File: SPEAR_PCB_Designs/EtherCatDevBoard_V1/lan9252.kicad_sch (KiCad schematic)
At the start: 29 parts, among them U4 LAN9252I/ML, Y2 25MHz

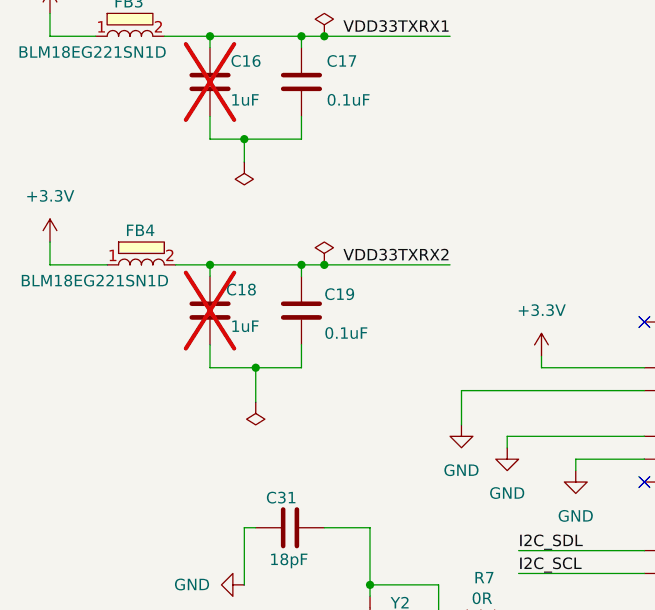
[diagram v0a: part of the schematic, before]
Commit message: Henry's continued work on the EtherCAT microcontroller dev. board.
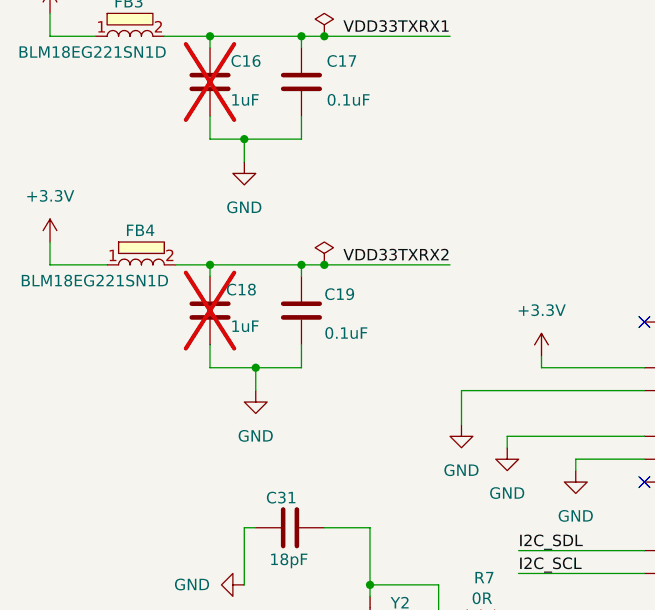
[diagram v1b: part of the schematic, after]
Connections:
- net GND: now also C16.2, C17.2, C18.2, C19.2
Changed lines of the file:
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@@
 	(wire
 		(pts
-			(xy 41.91 63.5) (xy 41.91 59.69)
+			(xy 41.91 62.23) (xy 41.91 59.69)
 		)
 		(stroke
@@
 	)
 	(symbol
-		(lib_id "power:PWR_FLAG")
-		(at 40.64 36.83 180)
-		(unit 1)
-		(exclude_from_sim no)
-		(in_bom yes)
-		(on_board yes)
-		(dnp no)
-		(fields_autoplaced yes)
-		(property "Reference" "#FLG06"
-			(at 40.64 38.735 0)
-			(effects
-				(font
-					(size 1.27 1.27)
-				)
-				(hide yes)
-			)
-		)
-		(property "Value" "PWR_FLAG"
-			(at 40.64 41.91 0)
-			(effects
-				(font
-					(size 1.27 1.27)
-				)
-				(hide yes)
-			)
-		)
-		(property "Footprint" ""
-			(at 40.64 36.83 0)
-			(effects
-				(font
-					(size 1.27 1.27)
-				)
-				(hide yes)
-			)
-		)
-		(property "Datasheet" "~"
-			(at 40.64 36.83 0)
-			(effects
-				(font
-					(size 1.27 1.27)
-				)
-				(hide yes)
-			)
-		)
-		(property "Description" "Special symbol for telling ERC where power comes from"
-			(at 40.64 36.83 0)
-			(effects
-				(font
-					(size 1.27 1.27)
-				)
-				(hide yes)
-			)
-		)
-		(pin "1"
-		)
-		(instances
-			(project "SPEAR_V1"
-				(path "/6af343d7-7346-4b6a-90ee-eb113982f4e5/d630782a-bbb8-450e-a52a-35375a587c4e"
-					(reference "#FLG06")
-					(unit 1)
-				)
-			)
-		)
-	)
-	(symbol
 		(lib_id "Device:C")
 		(at 231.14 63.5 0)
@@
 	)
 	(symbol
-		(lib_id "power:PWR_FLAG")
-		(at 41.91 63.5 180)
+		(lib_id "power:GND")
+		(at 40.64 36.83 0)
 		(unit 1)
 		(exclude_from_sim no)
@@
 		(dnp no)
 		(fields_autoplaced yes)
-		(property "Reference" "#FLG010"
-			(at 41.91 65.405 0)
+		(property "Reference" "#PWR059"
+			(at 40.64 43.18 0)
 			(effects
 				(font
@@
 			)
 		)
-		(property "Value" "PWR_FLAG"
-			(at 41.91 68.58 0)
+		(property "Value" "GND"
+			(at 40.64 41.91 0)
 			(effects
 				(font
 					(size 1.27 1.27)
 				)
-				(hide yes)
 			)
 		)
 		(property "Footprint" ""
-			(at 41.91 63.5 0)
+			(at 40.64 36.83 0)
 			(effects
 				(font
@@
 			)
 		)
-		(property "Datasheet" "~"
-			(at 41.91 63.5 0)
+		(property "Datasheet" ""
+			(at 40.64 36.83 0)
 			(effects
 				(font
@@
 			)
 		)
-		(property "Description" "Special symbol for telling ERC where power comes from"
-			(at 41.91 63.5 0)
+		(property "Description" "Power symbol creates a global label with name \"GND\" , ground"
+			(at 40.64 36.83 0)
 			(effects
 				(font
@@
 		)
 		(instances
-			(project "SPEAR_V1"
+			(project ""
 				(path "/6af343d7-7346-4b6a-90ee-eb113982f4e5/d630782a-bbb8-450e-a52a-35375a587c4e"
-					(reference "#FLG010")
+					(reference "#PWR059")
 					(unit 1)
 				)
@@
 					(unit 1)
 				)
+			)
+		)
+	)
+	(symbol
+		(lib_id "power:GND")
+		(at 41.91 62.23 0)
+		(unit 1)
+		(exclude_from_sim no)
+		(in_bom yes)
+		(on_board yes)
+		(dnp no)
+		(fields_autoplaced yes)
+		(property "Reference" "#PWR060"
+			(at 41.91 68.58 0)
+			(effects
+				(font
+					(size 1.27 1.27)
+				)
+				(hide yes)
+			)
+		)
+		(property "Value" "GND"
+			(at 41.91 67.31 0)
+			(effects
+				(font
+					(size 1.27 1.27)
+				)
+			)
+		)
+		(property "Footprint" ""
+			(at 41.91 62.23 0)
+			(effects
+				(font
+					(size 1.27 1.27)
+				)
+				(hide yes)
+			)
+		)
+		(property "Datasheet" ""
+			(at 41.91 62.23 0)
+			(effects
+				(font
+					(size 1.27 1.27)
+				)
+				(hide yes)
+			)
+		)
+		(property "Description" "Power symbol creates a global label with name \"GND\" , ground"
+			(at 41.91 62.23 0)
+			(effects
+				(font
+					(size 1.27 1.27)
+				)
+				(hide yes)
+			)
+		)
+		(pin "1"
+		)
+		(instances
+			(project "SPEAR_V1"
+				(path "/6af343d7-7346-4b6a-90ee-eb113982f4e5/d630782a-bbb8-450e-a52a-35375a587c4e"
+					(reference "#PWR060")
+					(unit 1)
+				)

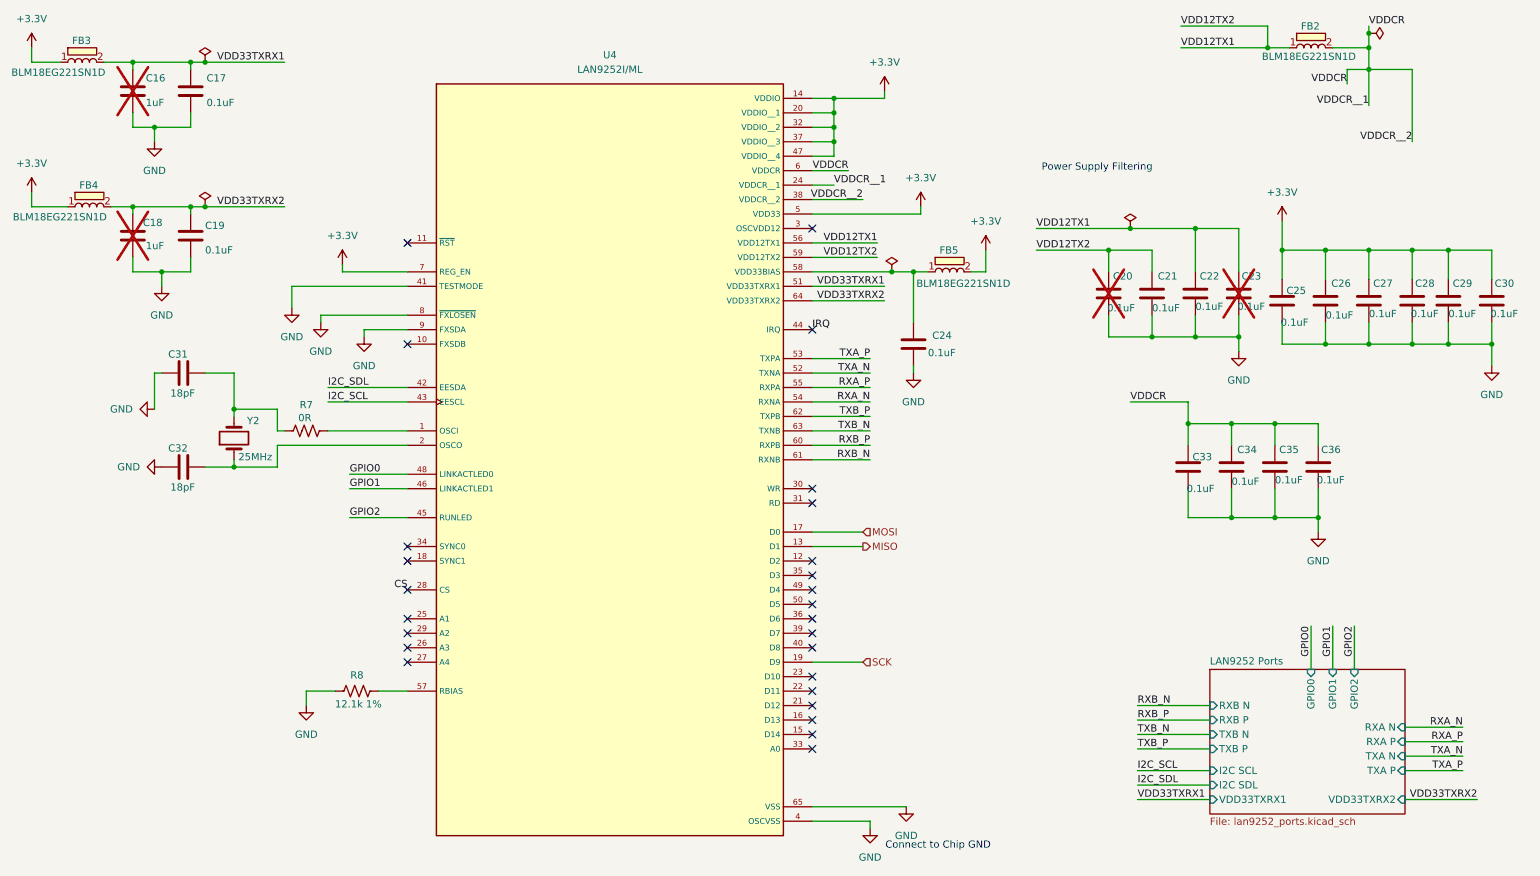
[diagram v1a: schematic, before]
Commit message: Edited schematic to fix problems with Lan9252. Continued work on pcb layout.
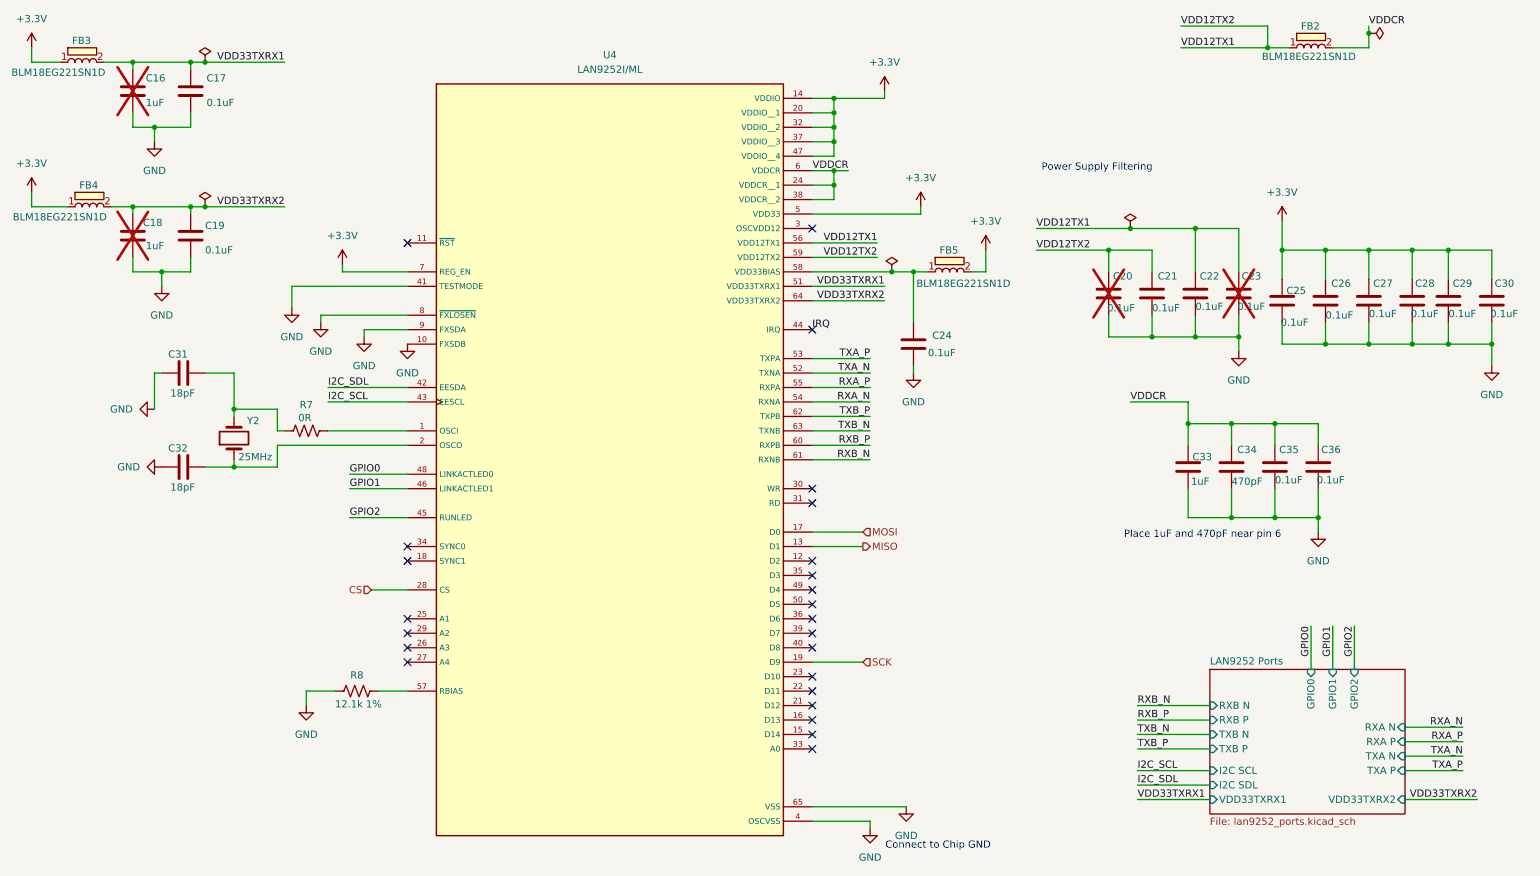
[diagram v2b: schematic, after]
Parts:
- C33: value 0.1uF -> 1uF
- C34: value 0.1uF -> 470pF
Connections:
- net GND: now also U4.10 (FXSDB)
- no-connect marks 26 -> 24
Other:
- note added: "Place 1uF and 470pF near pin 6"
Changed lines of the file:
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@@
 	(generator_version "9.0")
 	(paper "A4")
+	(text "Place 1uF and 470pF near pin 6"
+		(exclude_from_sim no)
+		(at 224.79 105.918 0)
+		(effects
+			(font
+				(size 1.27 1.27)
+			)
+		)
+	)
 	(text "Connect to Chip GND"
 		(exclude_from_sim no)
@@
 	)
 	(junction
-		(at 254 20.32)
-		(diameter 0)
-		(color 0 0 0 0)
-	)
-	(junction
-		(at 254 24.13)
-		(diameter 0)
-		(color 0 0 0 0)
-	)
-	(junction
 		(at 237.49 86.36)
 		(diameter 0)
@@
 	)
 	(junction
+		(at 160.02 44.45)
+		(diameter 0)
+		(color 0 0 0 0)
+	)
+	(junction
 		(at 46.99 22.86)
 		(diameter 0)
@@
 	)
 	(junction
+		(at 160.02 41.91)
+		(diameter 0)
+		(color 0 0 0 0)
+	)
+	(junction
 		(at 229.87 86.36)
 		(diameter 0)
@@
 	)
 	(no_connect
-		(at 85.09 115.57)
-	)
-	(no_connect
 		(at 156.21 115.57)
 	)
@@
 	)
 	(no_connect
-		(at 85.09 72.39)
-	)
-	(no_connect
 		(at 156.21 143.51)
 	)
@@
 	(wire
 		(pts
-			(xy 250.19 26.67) (xy 250.19 24.13)
-		)
-		(stroke
-			(width 0)
-			(type default)
-		)
-	)
-	(wire
-		(pts
 			(xy 40.64 36.83) (xy 40.64 34.29)
 		)
@@
 	(wire
 		(pts
+			(xy 78.74 115.57) (xy 85.09 115.57)
+		)
+		(stroke
+			(width 0)
+			(type default)
+		)
+	)
+	(wire
+		(pts
 			(xy 275.59 55.88) (xy 275.59 60.96)
 		)
@@
 	(wire
 		(pts
+			(xy 160.02 41.91) (xy 160.02 44.45)
+		)
+		(stroke
+			(width 0)
+			(type default)
+		)
+	)
+	(wire
+		(pts
 			(xy 213.36 149.86) (xy 226.06 149.86)
 		)
@@
 	(wire
 		(pts
-			(xy 165.1 46.99) (xy 156.21 46.99)
+			(xy 156.21 46.99) (xy 160.02 46.99)
 		)
 		(stroke
@@
 	(wire
 		(pts
-			(xy 261.62 24.13) (xy 261.62 36.83)
-		)
-		(stroke
-			(width 0)
-			(type default)
-		)
-	)
-	(wire
-		(pts
 			(xy 270.51 139.7) (xy 260.35 139.7)
 		)
@@
 	(wire
 		(pts
-			(xy 254 24.13) (xy 254 30.48)
-		)
-		(stroke
-			(width 0)
-			(type default)
-		)
-	)
-	(wire
-		(pts
 			(xy 40.64 34.29) (xy 46.99 34.29)
 		)
@@
 	(wire
 		(pts
+			(xy 160.02 46.99) (xy 160.02 44.45)
+		)
+		(stroke
+			(width 0)
+			(type default)
+		)
+	)
+	(wire
+		(pts
 			(xy 213.36 147.32) (xy 226.06 147.32)
 		)
@@
 	(wire
 		(pts
-			(xy 162.56 41.91) (xy 156.21 41.91)
+			(xy 162.56 41.91) (xy 160.02 41.91)
 		)
 		(stroke
@@
 	(wire
 		(pts
-			(xy 254 20.32) (xy 254 24.13)
-		)
-		(stroke
-			(width 0)
-			(type default)
-		)
-	)
-	(wire
-		(pts
 			(xy 46.99 48.26) (xy 46.99 49.53)
 		)
@@
 	(wire
 		(pts
-			(xy 254 24.13) (xy 261.62 24.13)
-		)
-		(stroke
-			(width 0)
-			(type default)
-		)
-	)
-	(wire
-		(pts
 			(xy 223.52 59.69) (xy 223.52 52.07)
 		)
@@
 	(wire
 		(pts
-			(xy 250.19 24.13) (xy 254 24.13)
+			(xy 246.38 55.88) (xy 246.38 60.96)
 		)
 		(stroke
@@
 	(wire
 		(pts
-			(xy 246.38 55.88) (xy 246.38 60.96)
+			(xy 222.25 102.87) (xy 229.87 102.87)
 		)
 		(stroke
@@
 	(wire
 		(pts
-			(xy 222.25 102.87) (xy 229.87 102.87)
+			(xy 54.61 77.47) (xy 54.61 83.82)
 		)
 		(stroke
@@
 	(wire
 		(pts
-			(xy 54.61 77.47) (xy 54.61 83.82)
+			(xy 165.1 128.27) (xy 156.21 128.27)
 		)
 		(stroke
@@
 	(wire
 		(pts
-			(xy 165.1 128.27) (xy 156.21 128.27)
+			(xy 247.65 121.92) (xy 247.65 129.54)
 		)
 		(stroke
@@
 	(wire
 		(pts
-			(xy 247.65 121.92) (xy 247.65 129.54)
+			(xy 46.99 34.29) (xy 46.99 31.75)
 		)
 		(stroke
@@
 	(wire
 		(pts
-			(xy 46.99 34.29) (xy 46.99 31.75)
+			(xy 160.02 41.91) (xy 156.21 41.91)
 		)
 		(stroke
@@
 		)
 	)
-	(label "VDDCR__2"
-		(at 261.62 36.83 180)
-		(effects
-			(font
-				(size 1.27 1.27)
-			)
-			(justify right bottom)
-		)
-	)
 	(label "RXB_N"
 		(at 166.37 92.71 180)
@@
 		)
 	)
-	(label "VDDCR"
-		(at 250.19 26.67 180)
-		(effects
-			(font
-				(size 1.27 1.27)
-			)
-			(justify right bottom)
-		)
-	)
-	(label "CS"
-		(at 85.09 115.57 180)
-		(effects
-			(font
-				(size 1.27 1.27)
-			)
-			(justify right bottom)
-		)
-	)
 	(label "RXB_P"
 		(at 213.36 138.43 0)
@@
 		)
 	)
-	(label "VDDCR__1"
-		(at 254 30.48 180)
-		(effects
-			(font
-				(size 1.27 1.27)
-			)
-			(justify right bottom)
-		)
-	)
 	(label "RXB_N"
 		(at 213.36 135.89 0)
@@
 		)
 	)
-	(label "VDDCR__1"
-		(at 160.02 44.45 0)
-		(effects
-			(font
-				(size 1.27 1.27)
-			)
-			(justify left bottom)
-		)
-	)
 	(label "TXA_P"
 		(at 270.51 147.32 180)
@@
 		)
 	)
-	(label "VDDCR__2"
-		(at 165.1 46.99 180)
-		(effects
-			(font
-				(size 1.27 1.27)
-			)
-			(justify right bottom)
-		)
-	)
 	(label "I2C_SDL"
 		(at 213.36 149.86 0)
@@
 		)
 	)
+	(hierarchical_label "CS"
+		(shape input)
+		(at 78.74 115.57 180)
+		(effects
+			(font
+				(size 1.27 1.27)
+			)
+			(justify right)
+		)
+	)
 	(hierarchical_label "MOSI"
 		(shape input)
@@
 			)
 		)
-		(property "Value" "0.1uF"
-			(at 221.996 97.79 0)
+		(property "Value" "1uF"
+			(at 222.758 96.52 0)
 			(effects
 				(font
@@
 			)
 		)
-		(property "Value" "0.1uF"
+		(property "Value" "470pF"
 			(at 229.87 96.52 0)
 			(effects
@@
 					(unit 1)
 				)
+			)
+		)
+	)
+	(symbol
+		(lib_id "power:GND")
+		(at 85.09 72.39 0)
+		(unit 1)
+		(exclude_from_sim no)
+		(in_bom yes)
+		(on_board yes)
+		(dnp no)
+		(fields_autoplaced yes)
+		(property "Reference" "#PWR068"
+			(at 85.09 78.74 0)
+			(effects
+				(font
+					(size 1.27 1.27)
+				)
+				(hide yes)
+			)
+		)
+		(property "Value" "GND"
+			(at 85.09 77.47 0)
+			(effects
+				(font
+					(size 1.27 1.27)
+				)
+			)
+		)
+		(property "Footprint" ""
+			(at 85.09 72.39 0)
+			(effects
+				(font
+					(size 1.27 1.27)
+				)
+				(hide yes)
+			)
+		)
+		(property "Datasheet" ""
+			(at 85.09 72.39 0)
+			(effects
+				(font
+					(size 1.27 1.27)
+				)
+				(hide yes)
+			)
+		)
+		(property "Description" "Power symbol creates a global label with name \"GND\" , ground"
+			(at 85.09 72.39 0)
+			(effects
+				(font
+					(size 1.27 1.27)
+				)
+				(hide yes)
+			)
+		)
+		(pin "1"
+		)
+		(instances
+			(project "SPEAR_V1"
+				(path "/6af343d7-7346-4b6a-90ee-eb113982f4e5/d630782a-bbb8-450e-a52a-35375a587c4e"
+					(reference "#PWR068")
+					(unit 1)
+				)

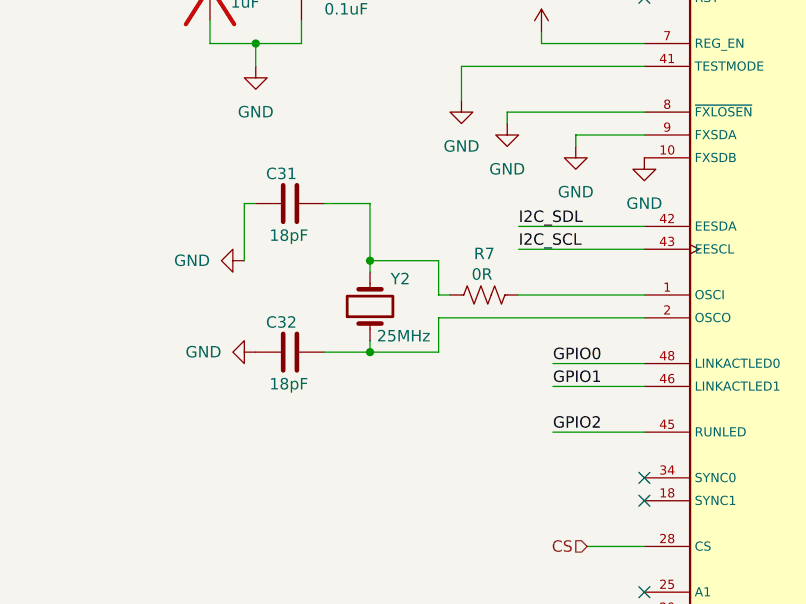
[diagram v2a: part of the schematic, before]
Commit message: Continued work on the PCB layout of the EtherCAT microcontroller dev board. Not complete yet.
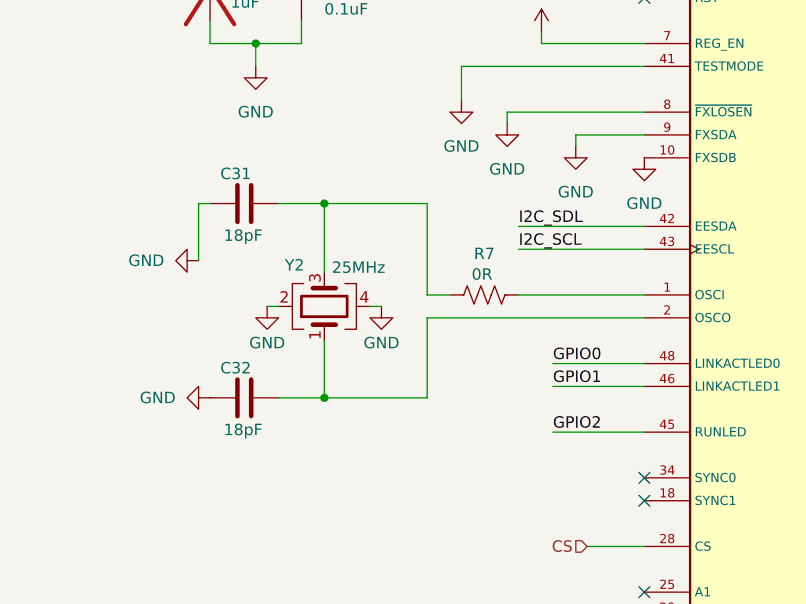
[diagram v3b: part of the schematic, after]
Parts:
- removed Y2: 25MHz, LAN9252 Footprints:Y_Wurth_WE-XTAL_Quartz-HC49-4HSMX, symbol Device:Crystal
- added Y2: 25MHz, Crystal:Crystal_SMD_Abracon_ABM8G-4Pin_3.2x2.5mm, symbol Device:Crystal_GND24
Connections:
- net GND: now also Y2.2, Y2.4
- net at C31.2, R7.1: now also Y2.3
- net at C32.2, U4.2 (OSCO): now also Y2.1
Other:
- moved on the sheet: C31, C32
